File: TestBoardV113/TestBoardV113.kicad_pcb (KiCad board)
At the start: 2 copper layers, 98 x 86 mm, 82 parts, among them J1 Conn_01x02_Pin, J10 Conn_01x02_Pin, J11 Conn_01x02_Pin, J12 Conn_01x02_Pin, J13 Conn_01x02_Pin, J14 Conn_02x03_Odd_Even, J15 Conn_01x01_Pin, J16 Conn_01x28_Socket, J17 Conn_01x01_Pin, J18 Conn_01x01_Pin, J19 Conn_01x02_Pin, J2 Conn_01x02_Socket, J20 Conn_01x02_Socket, J21 Conn_01x28_Socket, J22 Conn_01x01_Pin, J23 Conn_01x02_Pin, J24 Conn_02x03_Odd_Even, J25 Conn_01x02_Pin, J26 Conn_01x02_Socket, J3 Conn_02x03_Odd_Even, J4 Conn_02x06_Odd_Even, J5 Conn_01x02_Pin, J6 Conn_01x02_Pin, J7 Conn_01x02_Pin, J8 Conn_01x02_Pin, J9 Conn_01x02_Pin, SW1 SW_DIP_x04, U3 NCP705MTADJTCG, U4 TAR5SxxU_SOT353F, U5 TXB0104PW, U6 TXB0104PW

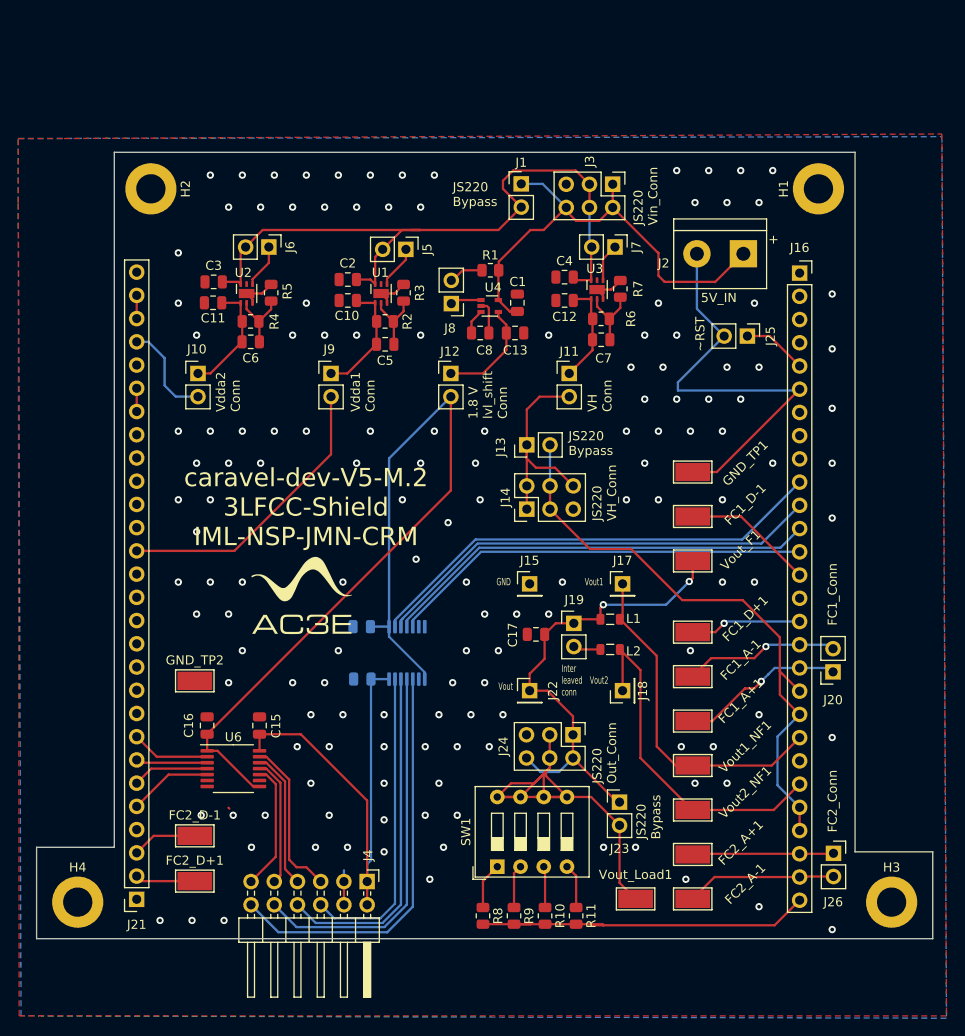
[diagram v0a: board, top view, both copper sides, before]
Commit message: Changed Items
Changed dip switch from 4
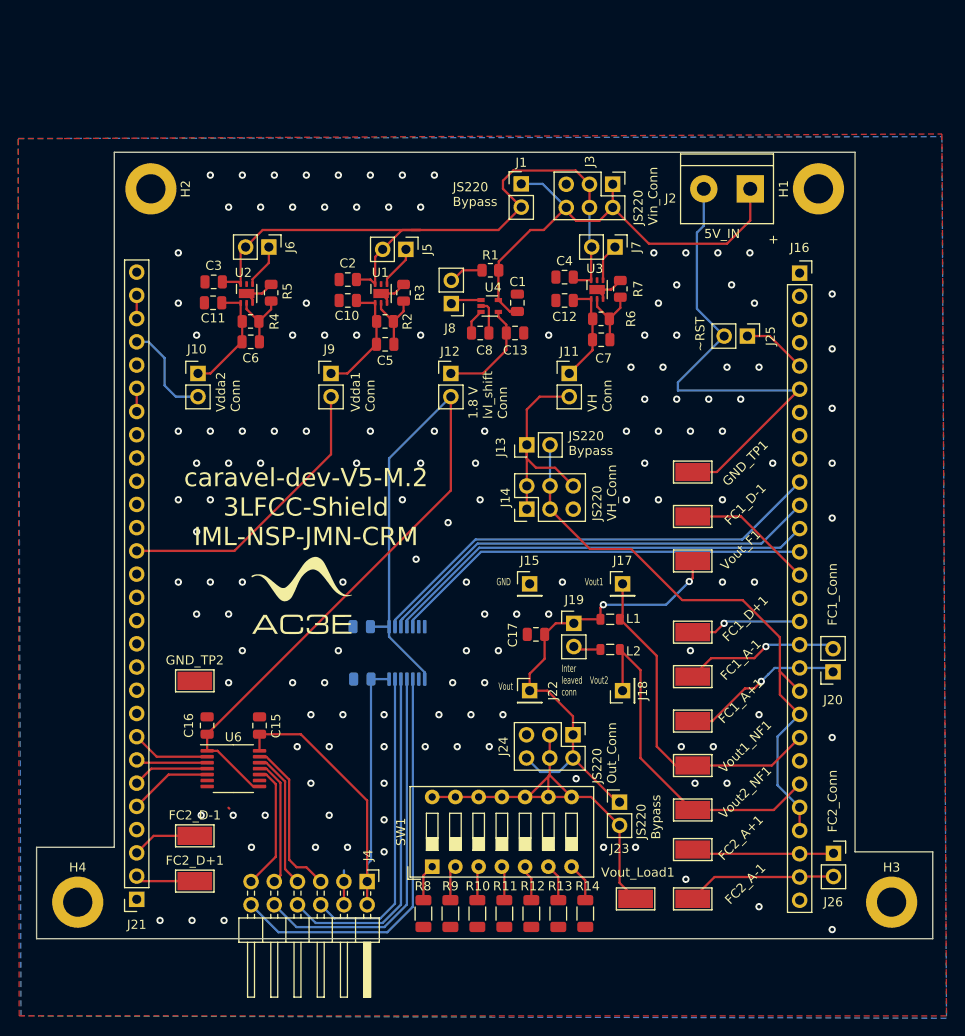
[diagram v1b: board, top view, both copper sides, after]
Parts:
- added R12: 330, Resistor_SMD:R_1206_3216Metric, F.Cu at (149.1, 127.8)
- added R13: 60, Resistor_SMD:R_1206_3216Metric, F.Cu at (152.1, 127.8)
- added R14: 30, Resistor_SMD:R_1206_3216Metric, F.Cu at (155.0, 127.8)
- R10, R11, R8, R9: footprint Resistor_SMD:R_0805_2012Metric -> Resistor_SMD:R_1206_3216Metric
- SW1: value SW_DIP_x04 -> SW_DIP_x07; footprint Button_Switch_THT:SW_DIP_SPSTx04_Slide_9.78x12.34mm_W7.62mm_P2.54mm -> Button_Switch_THT:SW_DIP_SPSTx07_Slide_9.78x19.96mm_W7.62mm_P2.54mm
- moved R11 7.85 mm to (146.2, 127.8)
- moved R10 7.41 mm to (143.2, 127.8)
- moved J2 7.14 mm to (173.0, 48.5)
- moved SW1 7.12 mm to (138.3, 122.6)
- moved R9 6.96 mm to (140.2, 127.8)
- moved R8 6.52 mm to (137.3, 127.8)
- moved FC2_A+1 0.53 mm to (166.8, 120.8)
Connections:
- SW1 pad 5: Load conection + -> Net-(R12-Pad1)
- SW1 pad 6: Load conection + -> Net-(R13-Pad1)
- SW1 pad 7: Load conection + -> Net-(R14-Pad1)
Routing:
- net GND: track 106.4 -> 74.9 mm, vias 143 -> 138
- net Load conection +: track 51.7 -> 44.5 mm
- net Net-(R14-Pad1): track 0.00 -> 4.29 mm
- net Net-(R13-Pad1): track 0.00 -> 4.12 mm
- net Net-(R12-Pad1): track 0.00 -> 3.95 mm
- net Net-(R11-Pad1): track 4.88 -> 3.78 mm
- net Net-(R8-Pad1): track 5.12 -> 4.07 mm
- net Net-(R9-Pad1): track 4.76 -> 3.90 mm
- net Net-(R10-Pad1): track 4.53 -> 3.73 mm
- net VCC: track 52.2 -> 52.9 mm
- net mprj_io[15]: track 16.4 -> 15.6 mm

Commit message: Changed Items
Added independent joulescope connection for vdda1 and 2, added testpoints for 1.8V pwm signals
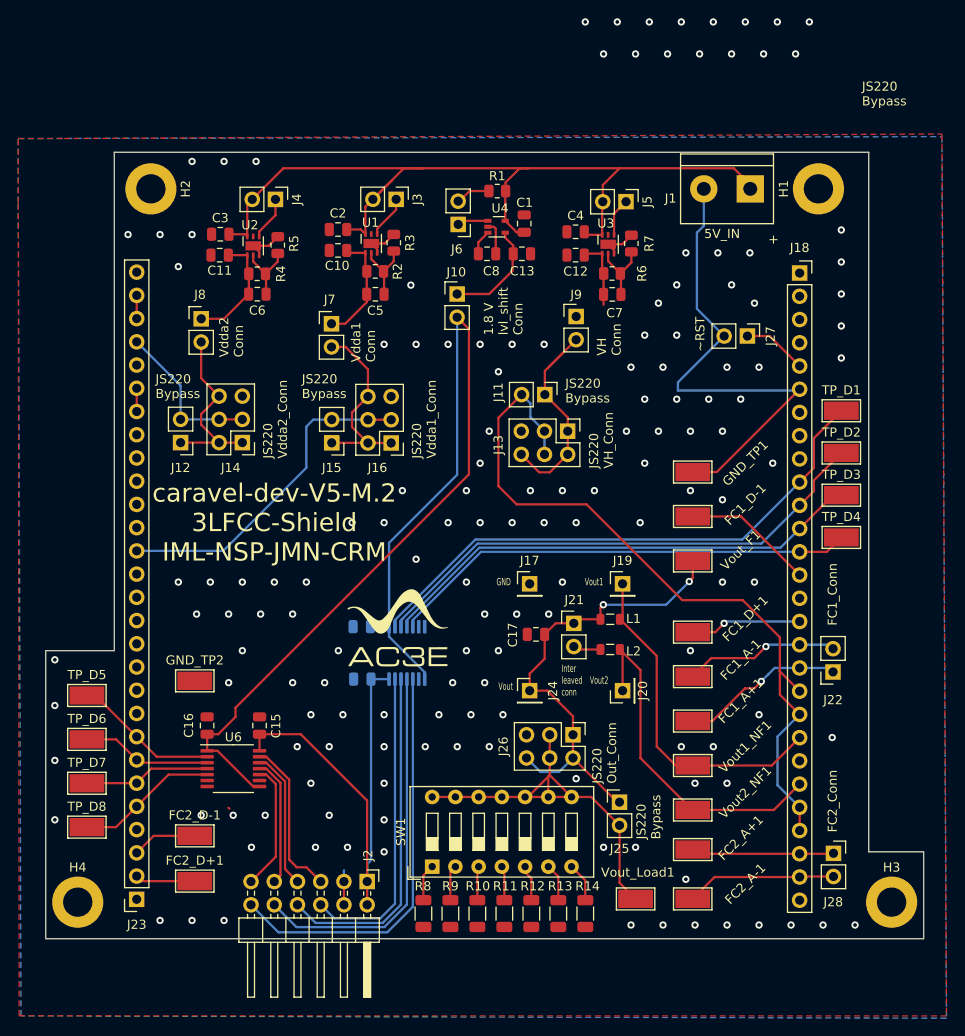
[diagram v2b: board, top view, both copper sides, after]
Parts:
- added J12: Conn_01x02_Pin, Connector_PinHeader_2.54mm:PinHeader_1x02_P2.54mm_Vertical, F.Cu at (110.8, 76.2)
- added J14: Conn_02x03_Odd_Even, Connector_PinHeader_2.54mm:PinHeader_2x03_P2.54mm_Vertical, F.Cu at (117.5, 76.2)
- added TP_D1: TestPoint, TestPoint:TestPoint_Keystone_5019_Minature, F.Cu at (183.0, 72.8)
- added TP_D2: TestPoint, TestPoint:TestPoint_Keystone_5019_Minature, F.Cu at (183.0, 77.4)
- added TP_D3: TestPoint, TestPoint:TestPoint_Keystone_5019_Minature, F.Cu at (183.0, 82.0)
- added TP_D4: TestPoint, TestPoint:TestPoint_Keystone_5019_Minature, F.Cu at (183.0, 86.6)
- added TP_D5: TestPoint, TestPoint:TestPoint_Keystone_5019_Minature, F.Cu at (100.5, 103.9)
- added TP_D6: TestPoint, TestPoint:TestPoint_Keystone_5019_Minature, F.Cu at (100.5, 108.7)
- added TP_D7: TestPoint, TestPoint:TestPoint_Keystone_5019_Minature, F.Cu at (100.5, 113.5)
- added TP_D8: TestPoint, TestPoint:TestPoint_Keystone_5019_Minature, F.Cu at (100.5, 118.3)
- moved J16 37.2 mm to (133.8, 76.3), turned to 180 degrees
- moved J15 35.1 mm to (127.3, 76.3), turned to 180 degrees
- moved G*** 11.1 mm to (134.5, 96.5)
- moved J13 9.63 mm to (153.1, 75.0), turned to -90 degrees
- moved J10 8.71 mm to (141.0, 60.0)
- moved C1 8.69 mm to (148.3, 52.3)
- moved C13 8.69 mm to (148.1, 55.6)
- moved C8 8.69 mm to (144.3, 55.6)
- moved R1 8.69 mm to (145.4, 48.7)
- moved U4 8.69 mm to (145.3, 52.6)
- moved J6 8.69 mm to (141.1, 52.4)
- moved J9 6.27 mm to (154.0, 62.5)
- moved J8 5.99 mm to (113.0, 62.7)
- moved J11 5.84 mm to (150.6, 71.0), turned to -90 degrees
- moved C10 5.58 mm to (128.0, 55.2)
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- renumbered J2 to J1, J12 to J10, J13 to J11, J14 to J13, J1 to J15, J3 to J16, J15 to J17, J16 to J18, J17 to J19, J4 to J2, J18 to J20, J19 to J21, J20 to J22, J21 to J23, J22 to J24, J23 to J25, J24 to J26, J25 to J27, J26 to J28, J5 to J3, J6 to J4, J7 to J5, J8 to J6, J9 to J7, J10 to J8, J11 to J9
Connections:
- C2 pad 1: VH/VDDA1-2_Power -> VCC
- C3 pad 1: VH/VDDA1-2_Power -> VCC
- C4 pad 1: VH/VDDA1-2_Power -> VCC
- J15 pad 1: VCC -> Net-(J15-Pin_1)
- J15 pad 2: VH/VDDA1-2_Power -> vdda1
- J16 pad 1: VCC -> Net-(J15-Pin_1)
- J16 pad 2: VCC -> Net-(J15-Pin_1)
- J16 pad 3: VH/VDDA1-2_Power -> vdda1
- J16 pad 4: VH/VDDA1-2_Power -> vdda1
- J16 pad 6: VCC -> Net-(J15-Pin_1)
- J3 pad 2: VH/VDDA1-2_Power -> VCC
- J4 pad 2: VH/VDDA1-2_Power -> VCC
- J5 pad 2: VH/VDDA1-2_Power -> VCC
- J7 pad 2: vdda1 -> Net-(J15-Pin_1)
- J8 pad 2: vdda2 -> Net-(J12-Pin_1)
- U1 pad 6: VH/VDDA1-2_Power -> VCC
- U2 pad 6: VH/VDDA1-2_Power -> VCC
- U3 pad 6: VH/VDDA1-2_Power -> VCC
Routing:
- net VH/VDDA1-2_Power: track 77.7 -> 0.00 mm
- net VCC: track 52.9 -> 100.2 mm
- net Net-(J15-Pin_1): track 0.00 -> 21.0 mm
- net Net-(J12-Pin_1): track 0.00 -> 20.2 mm
- net 1.8V-Shield: track 94.4 -> 114.2 mm
- net mprj_io[16]: track 65.2 -> 83.5 mm
- net mprj_io[31]: track 51.2 -> 60.9 mm
- net mprj_io[30]: track 49.7 -> 57.3 mm
- net mprj_io[7]: track 8.61 -> 15.9 mm
- net mprj_io[10]: track 9.15 -> 15.5 mm
- net mprj_io[8]: track 7.83 -> 14.2 mm
- net vdda2: track 10.9 -> 17.2 mm
- net mprj_io[29]: track 47.8 -> 53.9 mm
- net mprj_io[9]: track 8.36 -> 13.8 mm
- net mprj_io[28]: track 46.1 -> 51.3 mm
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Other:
- board size 98 x 86 mm -> 96 x 86 mm
- board text added: "JS220 Vdda1_Conn"
- board text added: "JS220 Vdda2_Conn"
- board text removed: "JS220 Vin_Conn"

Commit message: Minor errors
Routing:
- net Net-(J9-Pin_1): track 7.70 -> 11.1 mm
- net VCC: track 100.2 -> 97.2 mm
- net Net-(J11-Pin_1): track 23.8 -> 21.7 mm
- net GND: vias 150 -> 135
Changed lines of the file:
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@@
-    (effects (font (size 1 1) (thickness 0.15)) (justify left bottom))
-  )
-  (gr_text "JS220\nBypass" (at 185.25 39.5) (layer "F.SilkS" knockout)
     (effects (font (size 1 1) (thickness 0.15)) (justify left bottom))
   )
@@
   (segment (start 128.911 52.9485) (end 130.4535 52.9485) (width 0.25) (layer "F.Cu") (net 1))
   (segment (start 171.25 46.25) (end 158.75 46.25) (width 0.25) (layer "F.Cu") (net 1))
-  (segment (start 131.776 49.6465) (end 133.894 47.5285) (width 0.25) (layer "F.Cu") (net 1))
   (segment (start 147.5 53.25) (end 146.25 52) (width 0.25) (layer "F.Cu") (net 1))
   (segment (start 146.2875 47.8025) (end 146.2875 48.744) (width 0.25) (layer "F.Cu") (net 1))
@@
   (via (at 183 53) (size 0.8) (drill 0.4) (layers "F.Cu" "B.Cu") (free) (net 2))
   (via (at 142 99) (size 0.8) (drill 0.4) (layers "F.Cu" "B.Cu") (free) (net 2))
-  (via (at 176 30.25) (size 0.8) (drill 0.4) (layers "F.Cu" "B.Cu") (free) (net 2))
   (via (at 173.5 91.5) (size 0.8) (drill 0.4) (layers "F.Cu" "B.Cu") (free) (net 2))
   (via (at 133 113.5) (size 0.8) (drill 0.4) (layers "F.Cu" "B.Cu") (free) (net 2))
@@
   (via (at 150.5 85) (size 0.8) (drill 0.4) (layers "F.Cu" "B.Cu") (free) (net 2))
   (via (at 142 91.5) (size 0.8) (drill 0.4) (layers "F.Cu" "B.Cu") (free) (net 2))
-  (via (at 158.5 30.25) (size 0.8) (drill 0.4) (layers "F.Cu" "B.Cu") (free) (net 2))
-  (via (at 155 30.25) (size 0.8) (drill 0.4) (layers "F.Cu" "B.Cu") (free) (net 2))
   (via (at 136.5 89) (size 0.8) (drill 0.4) (layers "F.Cu" "B.Cu") (free) (net 2))
-  (via (at 157 33.75) (size 0.8) (drill 0.4) (layers "F.Cu" "B.Cu") (free) (net 2))
   (via (at 165 64.5) (size 0.8) (drill 0.4) (layers "F.Cu" "B.Cu") (free) (net 2))
   (via (at 165.5 109.5) (size 0.8) (drill 0.4) (layers "F.Cu" "B.Cu") (free) (net 2))
@@
   (via (at 159.5 75) (size 0.8) (drill 0.4) (layers "F.Cu" "B.Cu") (free) (net 2))
   (via (at 161.5 78.5) (size 0.8) (drill 0.4) (layers "F.Cu" "B.Cu") (free) (net 2))
-  (via (at 172.5 30.25) (size 0.8) (drill 0.4) (layers "F.Cu" "B.Cu") (free) (net 2))
   (via (at 125.5 120.5) (size 0.8) (drill 0.4) (layers "F.Cu" "B.Cu") (free) (net 2))
   (via (at 177.5 129) (size 0.8) (drill 0.4) (layers "F.Cu" "B.Cu") (free) (net 2))
@@
   (via (at 127 117) (size 0.8) (drill 0.4) (layers "F.Cu" "B.Cu") (free) (net 2))
   (via (at 174 129) (size 0.8) (drill 0.4) (layers "F.Cu" "B.Cu") (free) (net 2))
-  (via (at 178 33.75) (size 0.8) (drill 0.4) (layers "F.Cu" "B.Cu") (free) (net 2))
   (via (at 160 68) (size 0.8) (drill 0.4) (layers "F.Cu" "B.Cu") (free) (net 2))
   (via (at 118.5 120.5) (size 0.8) (drill 0.4) (layers "F.Cu" "B.Cu") (free) (net 2))
@@
   (via (at 123 102.5) (size 0.8) (drill 0.4) (layers "F.Cu" "B.Cu") (free) (net 2))
   (via (at 184.5 129) (size 0.8) (drill 0.4) (layers "F.Cu" "B.Cu") (free) (net 2))
-  (via (at 167.5 33.75) (size 0.8) (drill 0.4) (layers "F.Cu" "B.Cu") (free) (net 2))
   (via (at 149 81.5) (size 0.8) (drill 0.4) (layers "F.Cu" "B.Cu") (free) (net 2))
-  (via (at 164 33.75) (size 0.8) (drill 0.4) (layers "F.Cu" "B.Cu") (free) (net 2))
   (via (at 151 95) (size 0.8) (drill 0.4) (layers "F.Cu" "B.Cu") (free) (net 2))
   (via (at 183 63.5) (size 0.8) (drill 0.4) (layers "F.Cu" "B.Cu") (free) (net 2))
   (via (at 140.5 102.5) (size 0.8) (drill 0.4) (layers "F.Cu" "B.Cu") (free) (net 2))
   (via (at 144.5 75) (size 0.8) (drill 0.4) (layers "F.Cu" "B.Cu") (free) (net 2))
-  (via (at 162 30.25) (size 0.8) (drill 0.4) (layers "F.Cu" "B.Cu") (free) (net 2))
   (via (at 125 106) (size 0.8) (drill 0.4) (layers "F.Cu" "B.Cu") (free) (net 2))
   (via (at 170.5 113.5) (size 0.8) (drill 0.4) (layers "F.Cu" "B.Cu") (free) (net 2))
@@
   (via (at 133 109.5) (size 0.8) (drill 0.4) (layers "F.Cu" "B.Cu") (free) (net 2))
   (via (at 161.5 71.5) (size 0.8) (drill 0.4) (layers "F.Cu" "B.Cu") (free) (net 2))
-  (via (at 169 30.25) (size 0.8) (drill 0.4) (layers "F.Cu" "B.Cu") (free) (net 2))
   (via (at 165 59) (size 0.8) (drill 0.4) (layers "F.Cu" "B.Cu") (free) (net 2))
   (via (at 168.5 71.5) (size 0.8) (drill 0.4) (layers "F.Cu" "B.Cu") (free) (net 2))
@@
   (via (at 114 91.5) (size 0.8) (drill 0.4) (layers "F.Cu" "B.Cu") (free) (net 2))
   (via (at 152.5 81.5) (size 0.8) (drill 0.4) (layers "F.Cu" "B.Cu") (free) (net 2))
-  (via (at 174.5 33.75) (size 0.8) (drill 0.4) (layers "F.Cu" "B.Cu") (free) (net 2))
-  (via (at 179.5 30.25) (size 0.8) (drill 0.4) (layers "F.Cu" "B.Cu") (free) (net 2))
   (via (at 97 117.5) (size 0.8) (drill 0.4) (layers "F.Cu" "B.Cu") (free) (net 2))
   (via (at 147 85) (size 0.8) (drill 0.4) (layers "F.Cu" "B.Cu") (free) (net 2))
@@
   (via (at 135.929 59.0285) (size 0.8) (drill 0.4) (layers "F.Cu" "B.Cu") (free) (net 2))
   (via (at 112 128.5) (size 0.8) (drill 0.4) (layers "F.Cu" "B.Cu") (free) (net 2))
-  (via (at 171 33.75) (size 0.8) (drill 0.4) (layers "F.Cu" "B.Cu") (free) (net 2))
   (via (at 170.5 129) (size 0.8) (drill 0.4) (layers "F.Cu" "B.Cu") (free) (net 2))
-  (via (at 160.5 33.75) (size 0.8) (drill 0.4) (layers "F.Cu" "B.Cu") (free) (net 2))
   (via (at 163.5 129) (size 0.8) (drill 0.4) (layers "F.Cu" "B.Cu") (free) (net 2))
   (via (at 144 95) (size 0.8) (drill 0.4) (layers "F.Cu" "B.Cu") (free) (net 2))
   (via (at 117.5 91.5) (size 0.8) (drill 0.4) (layers "F.Cu" "B.Cu") (free) (net 2))
-  (via (at 165.5 30.25) (size 0.8) (drill 0.4) (layers "F.Cu" "B.Cu") (free) (net 2))
   (segment (start 165.13 70.55) (end 178.3032 70.55) (width 0.25) (layer "B.Cu") (net 2))
   (segment (start 128.61 124.25) (end 128.61 123.022) (width 0.25) (layer "B.Cu") (net 2))
@@
   (segment (start 152.5 66.5) (end 154 65) (width 0.25) (layer "F.Cu") (net 7))
   (segment (start 149.96 79.5) (end 151.12 79.5) (width 0.25) (layer "F.Cu") (net 7))
-  (segment (start 151 68) (end 152.5 66.5) (width 0.25) (layer "F.Cu") (net 7))
   (segment (start 150.58 68.42) (end 152.5 66.5) (width 0.25) (layer "F.Cu") (net 7))
   (segment (start 118.18975 60.018) (end 115.49775 62.71) (width 0.25) (layer "F.Cu") (net 8))
@@
   (segment (start 118.02825 55.75) (end 118.03975 55.7615) (width 0.25) (layer "F.Cu") (net 8))
   (segment (start 118.03975 55.7615) (end 118.03975 57.6225) (width 0.25) (layer "F.Cu") (net 8))
-  (segment (start 157 60.0425) (end 157 61.1845) (width 0.25) (layer "F.Cu") (net 9))
+  (segment (start 157 60.0425) (end 157 61) (width 0.25) (layer "F.Cu") (net 9))
+  (segment (start 155.54 62.46) (end 157 61) (width 0.25) (layer "F.Cu") (net 9))
   (segment (start 155.0565 55.586) (end 154.894 55.7485) (width 0.25) (layer "F.Cu") (net 9))
+  (segment (start 154 62.46) (end 155.54 62.46) (width 0.25) (layer "F.Cu") (net 9))
   (segment (start 156.85 55.586) (end 156.85 57.589) (width 0.25) (layer "F.Cu") (net 9))
   (segment (start 156.85 57.589) (end 157.0175 57.7565) (width 0.25) (layer "F.Cu") (net 9))
